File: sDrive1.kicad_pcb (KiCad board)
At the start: 2 copper layers, 50.1 x 35.5 mm, 34 parts, among them U1 DRV8323SRTAT, U2 24LC01

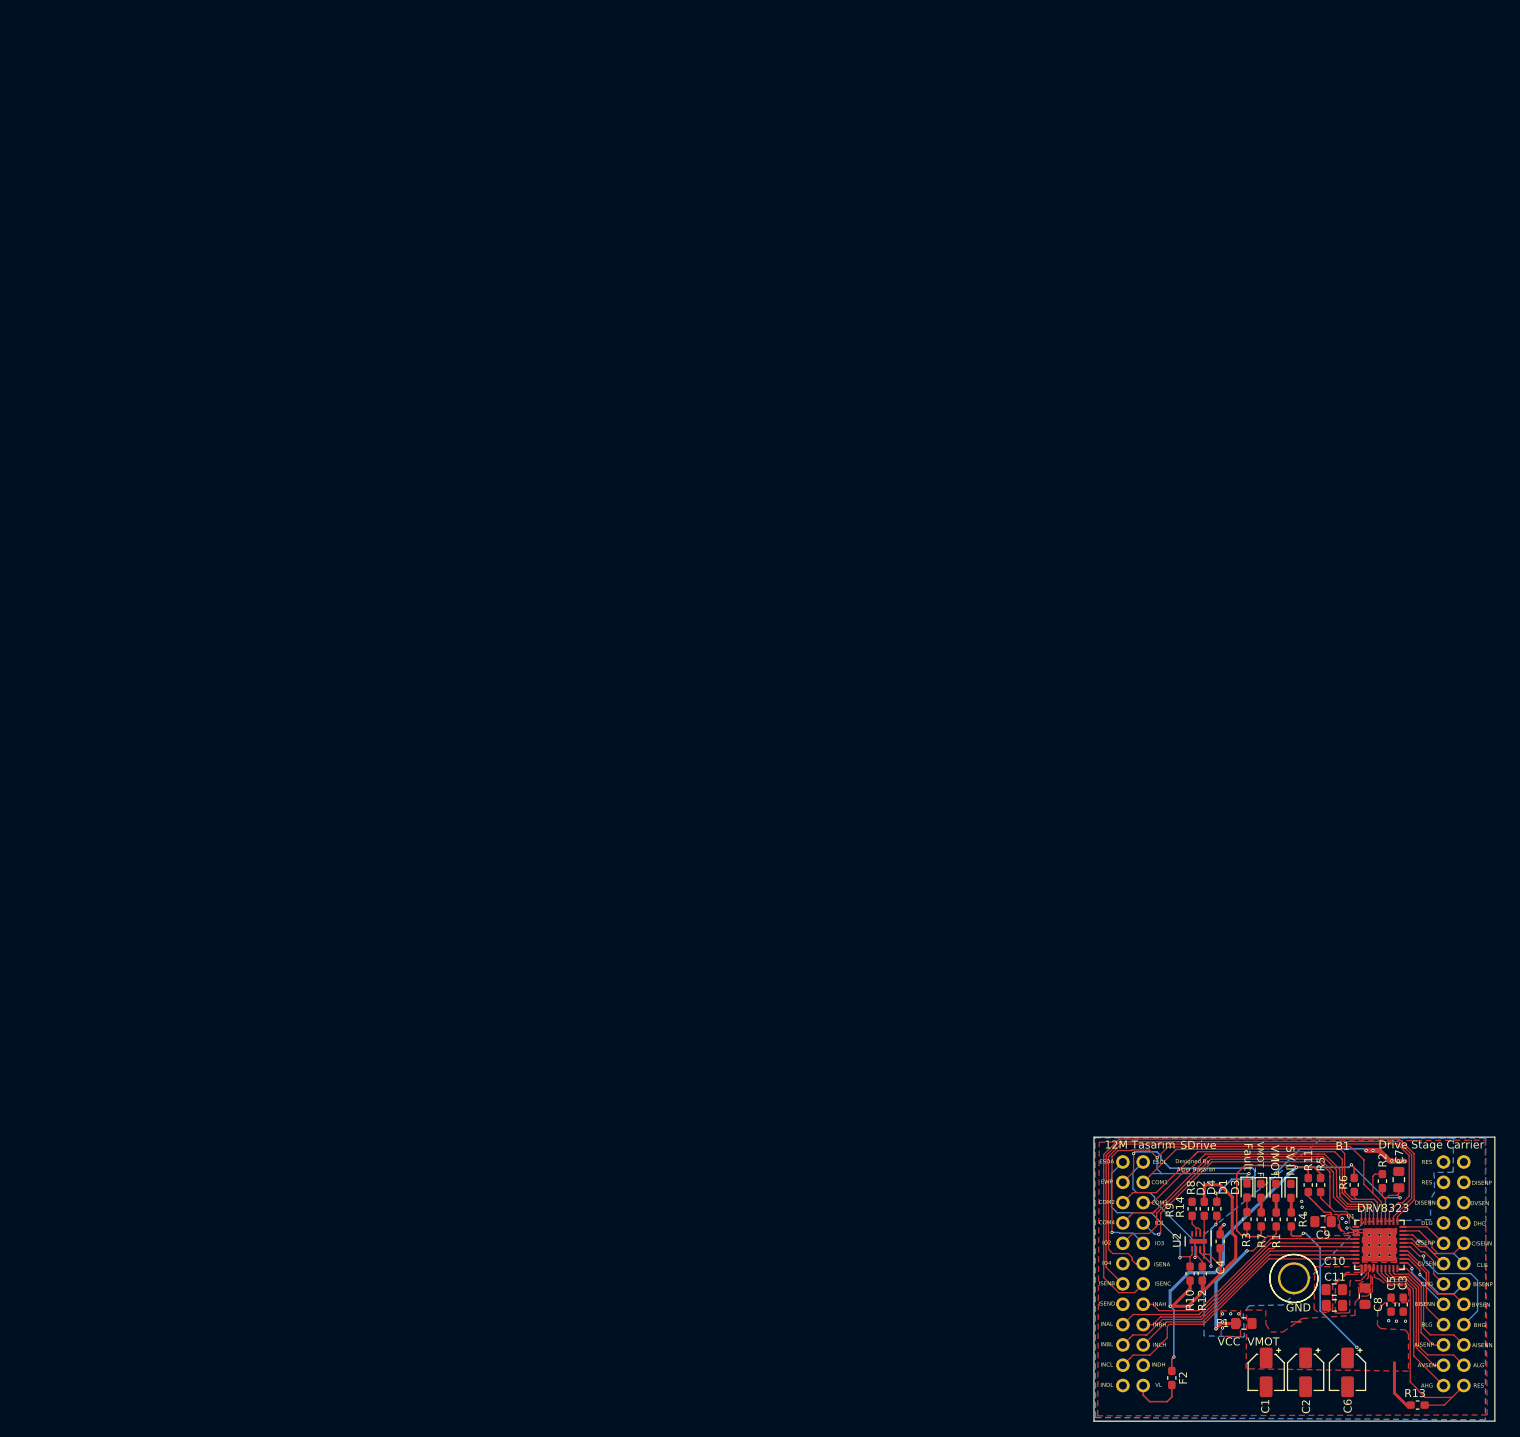
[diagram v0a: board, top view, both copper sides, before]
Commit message: update pcb layout
set board cutout
update eeprom footporint
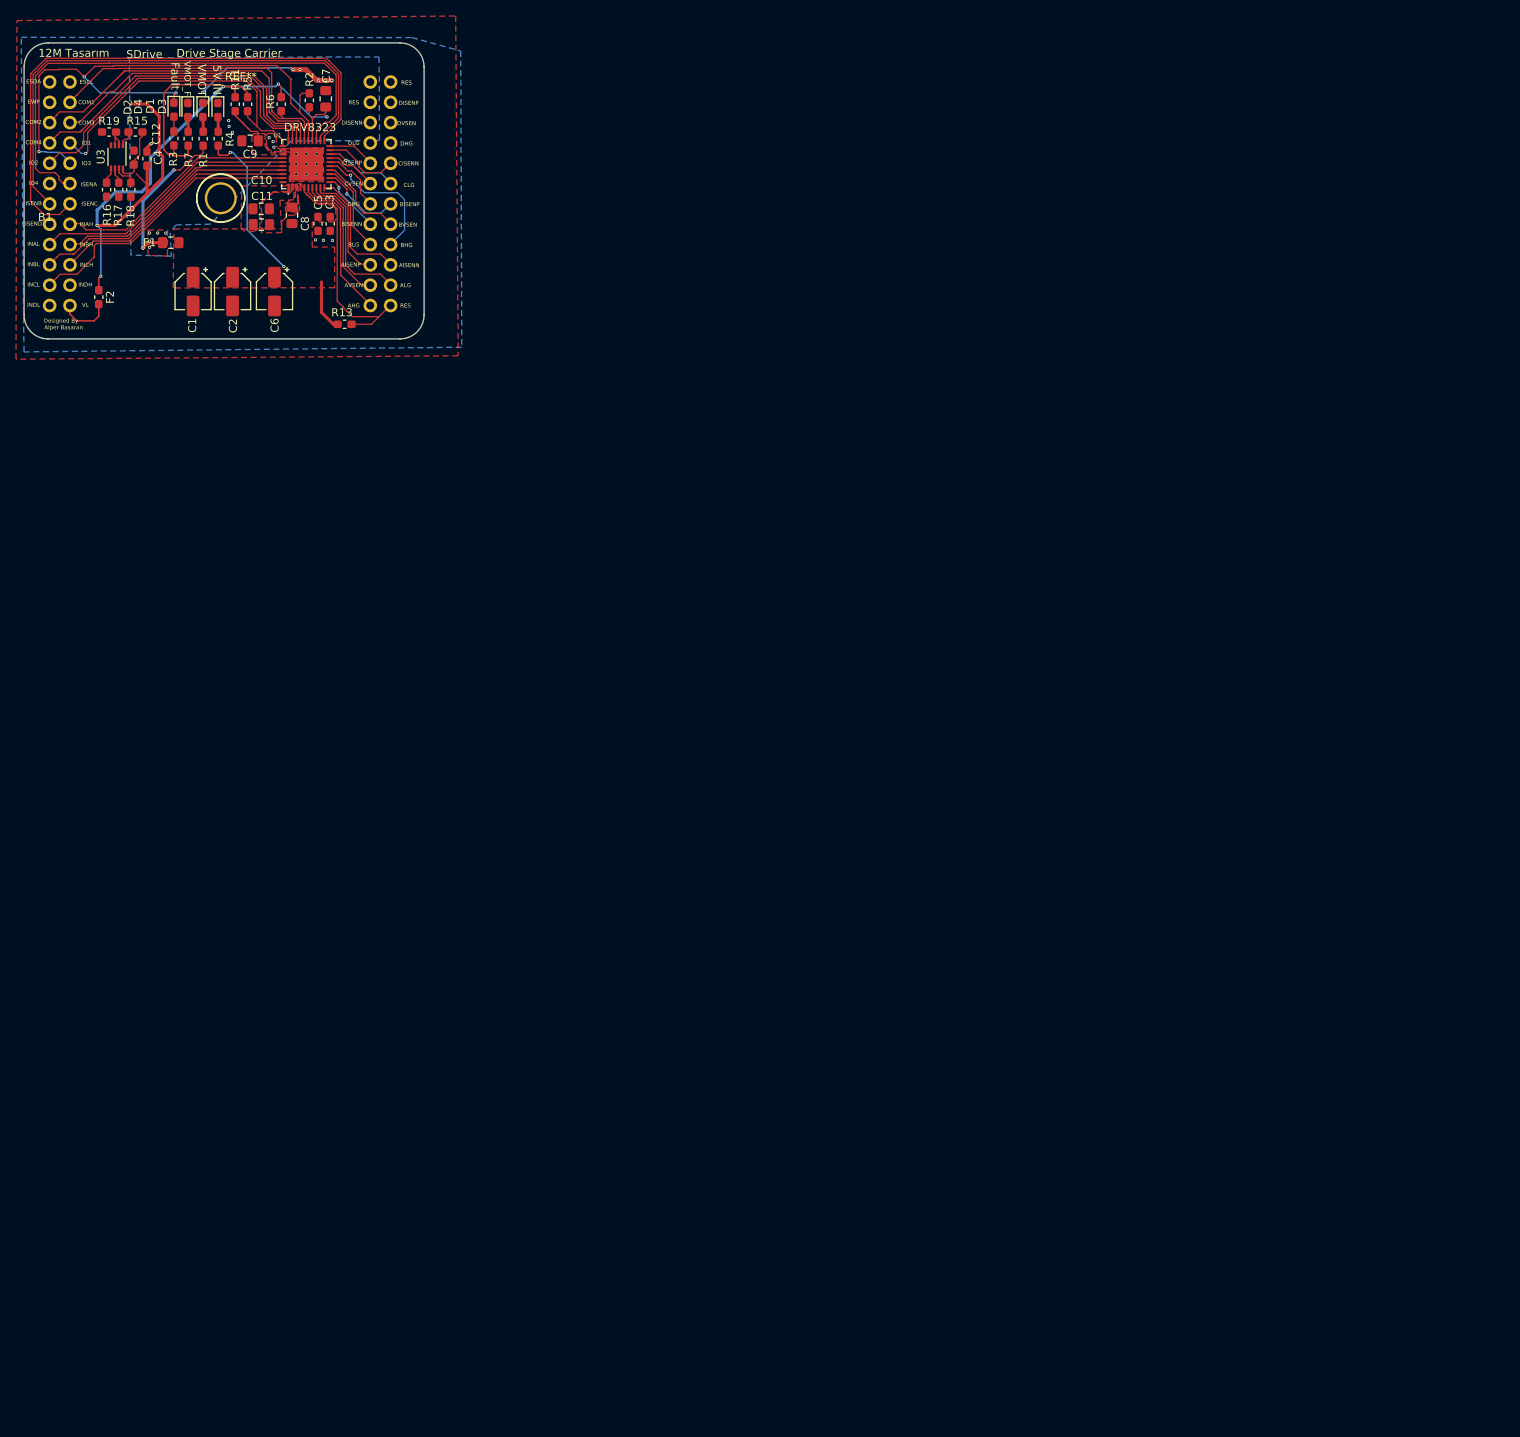
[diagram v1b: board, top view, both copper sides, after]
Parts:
- removed R10, R12, R14, R8, R9: R, Resistor_SMD:R_0603_1608Metric_Pad1.05x0.95mm_HandSolder
- removed U2: 24LC01, Package_DFN_QFN:DFN-8-1EP_2x3mm_P0.5mm_EP0.61x2.2mm
- added C12: X7R, 47-nF, Capacitor_SMD:C_0603_1608Metric_Pad1.05x0.95mm_HandSolder, F.Cu at (13.3, -22.4)
- added R15: R, Resistor_SMD:R_0603_1608Metric_Pad1.05x0.95mm_HandSolder, F.Cu at (13.5, -25.6)
- added R16: R, Resistor_SMD:R_0603_1608Metric_Pad1.05x0.95mm_HandSolder, F.Cu at (9.86, -18.3)
- added R17: R, Resistor_SMD:R_0603_1608Metric_Pad1.05x0.95mm_HandSolder, F.Cu at (11.4, -18.3)
- added R18: R, Resistor_SMD:R_0603_1608Metric_Pad1.05x0.95mm_HandSolder, F.Cu at (12.9, -18.3)
- added R19: R, Resistor_SMD:R_0603_1608Metric_Pad1.05x0.95mm_HandSolder, F.Cu at (10.2, -25.6)
- added U3: 24LC01, Package_DFN_QFN:DFN-8-1EP_3x2mm_P0.5mm_EP1.3x1.5mm, F.Cu at (11.2, -22.5)
- moved B1 197.3 mm to (-0.36, 0.33)
- moved C4 190.6 mm to (14.9, -22.2)
- moved C1 190.4 mm to (20.7, -5.61)
- moved C10 190.4 mm to (29.2, -16.0)
- moved C2 190.4 mm to (25.6, -5.61)
- moved C6 190.4 mm to (30.8, -5.61)
- moved D1 190.4 mm to (21.9, -28.3)
- moved D3 190.4 mm to (23.8, -28.3)
- moved D4 190.4 mm to (20.0, -28.3)
- moved R13 190.4 mm to (39.6, -1.52)
- moved R5 190.4 mm to (27.5, -29.0)
- moved C11 190.4 mm to (29.2, -14.0)
- moved C3 190.4 mm to (37.8, -14.1)
- moved C5 190.4 mm to (36.3, -14.1)
- moved C7 190.4 mm to (37.2, -29.7)
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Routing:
- net /Drive_Stage/WP: track 28.2 -> 0.00 mm, vias 2 -> 0
- net /Drive_Stage/SDA: track 22.3 -> 0.00 mm, vias 1 -> 0
- net /Drive_Stage/SCL: track 19.5 -> 0.00 mm, vias 1 -> 0
- net Net-(R14-Pad2): track 9.80 -> 0.00 mm, vias 2 -> 0
- net /Drive_Stage/5V_IN: track 121.6 -> 112.6 mm
- net /eeprom/5V_IN: track 0.00 -> 7.40 mm
- net Net-(R8-Pad1): track 3.57 -> 0.00 mm
- net Net-(R18-Pad2): track 0.00 -> 2.92 mm
- net Net-(R19-Pad1): track 0.00 -> 2.91 mm
- net Net-(R9-Pad2): track 2.27 -> 0.00 mm
- net Net-(R15-Pad2): track 0.00 -> 2.13 mm
- net /Drive_Stage/nFAULT: track 75.3 -> 73.2 mm
- net /eeprom/SDA: track 0.00 -> 2.01 mm
- net /eeprom/SCL: track 0.00 -> 1.98 mm
- net /Drive_Stage/SOC: track 71.2 -> 71.8 mm
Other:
- board size 50.1 x 35.5 mm -> 50 x 37 mm

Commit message: add production files
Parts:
- removed C4: X7R, 47-nF, Capacitor_SMD:C_0603_1608Metric_Pad1.05x0.95mm_HandSolder
- added D5: D_Schottky, Diode_SMD:D_0603_1608Metric_Pad1.05x0.95mm_HandSolder, F.Cu at (11.2, -8.38)
- moved F2 2.30 mm to (11.2, -4.91)
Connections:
- B1 pad 1: /Drive_Stage/SDA -> /Drive_Stage/EEPROM_SDA
- B1 pad 2: /Drive_Stage/SCL -> /Drive_Stage/EEPROM_SCL
- B1 pad 3: /Drive_Stage/WP -> /Drive_Stage/EEPROM_WP
- B1 pad 50: (no net) -> GND
- C12 pad 1: /eeprom/5V_IN -> /Drive_Stage/5V
- C7 pad 1: /Drive_Stage/5V_IN -> /Drive_Stage/5V
- F2 pad 1: /Drive_Stage/5V_IN -> Net-(D5-Pad2)
- R11 pad 1: /Drive_Stage/5V_IN -> /Drive_Stage/5V
- R15 pad 1: /eeprom/5V_IN -> /Drive_Stage/5V
- R16 pad 1: /eeprom/5V_IN -> /Drive_Stage/5V
- R16 pad 2: /eeprom/SDA -> /Drive_Stage/EEPROM_SDA
- R17 pad 1: /eeprom/5V_IN -> /Drive_Stage/5V
- R17 pad 2: /eeprom/SCL -> /Drive_Stage/EEPROM_SCL
- R18 pad 1: /eeprom/WP -> /Drive_Stage/EEPROM_WP
- R2 pad 1: /Drive_Stage/5V_IN -> /Drive_Stage/5V
- R3 pad 1: /Drive_Stage/5V_IN -> /Drive_Stage/5V
- R5 pad 1: /Drive_Stage/5V_IN -> /Drive_Stage/5V
- R6 pad 1: /Drive_Stage/5V_IN -> /Drive_Stage/5V
- R7 pad 1: /Drive_Stage/5V_IN -> /Drive_Stage/5V
- U1 pad 24: /Drive_Stage/5V_IN -> /Drive_Stage/5V
- U3 pad 5: /eeprom/SDA -> /Drive_Stage/EEPROM_SDA
- U3 pad 6: /eeprom/SCL -> /Drive_Stage/EEPROM_SCL
- U3 pad 8: /eeprom/5V_IN -> /Drive_Stage/5V
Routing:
- net /Drive_Stage/5V: track 0.00 -> 124.0 mm, vias 0 -> 6
- net /Drive_Stage/5V_IN: track 112.6 -> 0.00 mm, vias 5 -> 0
- net /Drive_Stage/EEPROM_WP: track 0.00 -> 23.3 mm, vias 0 -> 1
- net /Drive_Stage/EEPROM_SDA: track 0.00 -> 17.2 mm, vias 0 -> 1
- net GND: track 19.5 -> 35.0 mm, vias 16 -> 13
- net /Drive_Stage/EEPROM_SCL: track 0.00 -> 15.5 mm, vias 0 -> 1
- net /eeprom/5V_IN: track 7.40 -> 0.00 mm
- net /Drive_Stage/5V_IN_RAW: track 6.95 -> 9.09 mm
- net /eeprom/SDA: track 2.01 -> 0.00 mm
- net /eeprom/SCL: track 1.98 -> 0.00 mm
- net Net-(D5-Pad2): track 0.00 -> 1.72 mm
